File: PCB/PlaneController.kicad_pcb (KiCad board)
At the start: 2 copper layers, 48.3 x 86.4 mm, 12 parts, among them J1 Conn_01x06_Pin, J2 Conn_01x04_Pin, J3 Conn_01x02, M2 Motor_Servo, M3 Motor_Servo, M4 Motor_Servo, M5 Motor_Servo

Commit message: Add 5th servo
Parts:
- added M1: Motor_Servo, Connector_PinHeader_2.54mm:PinHeader_1x03_P2.54mm_Vertical, F.Cu at (96.5, 73.7)
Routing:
- net Net-(A1-D2): track 0.00 -> 12.1 mm
- net Net-(J1-Pin_3): track 166.3 -> 170.7 mm
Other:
- board text added: "D2"

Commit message: Add RX and TX connections to connect to receiver via iBUS
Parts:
- added J4: Conn_01x02, Connector_PinHeader_2.54mm:PinHeader_1x02_P2.54mm_Vertical, F.Cu at (91.4, 99.1)
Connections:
- A1 pad 1: unconnected-(A1-TX1-Pad1) -> Net-(A1-TX1)
- A1 pad 2: unconnected-(A1-RX1-Pad2) -> Net-(A1-RX1)
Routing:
- net Net-(A1-RX1): track 0.00 -> 58.4 mm
- net Net-(A1-TX1): track 0.00 -> 30.9 mm
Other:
- board text added: "RX"
- board text added: "TX"

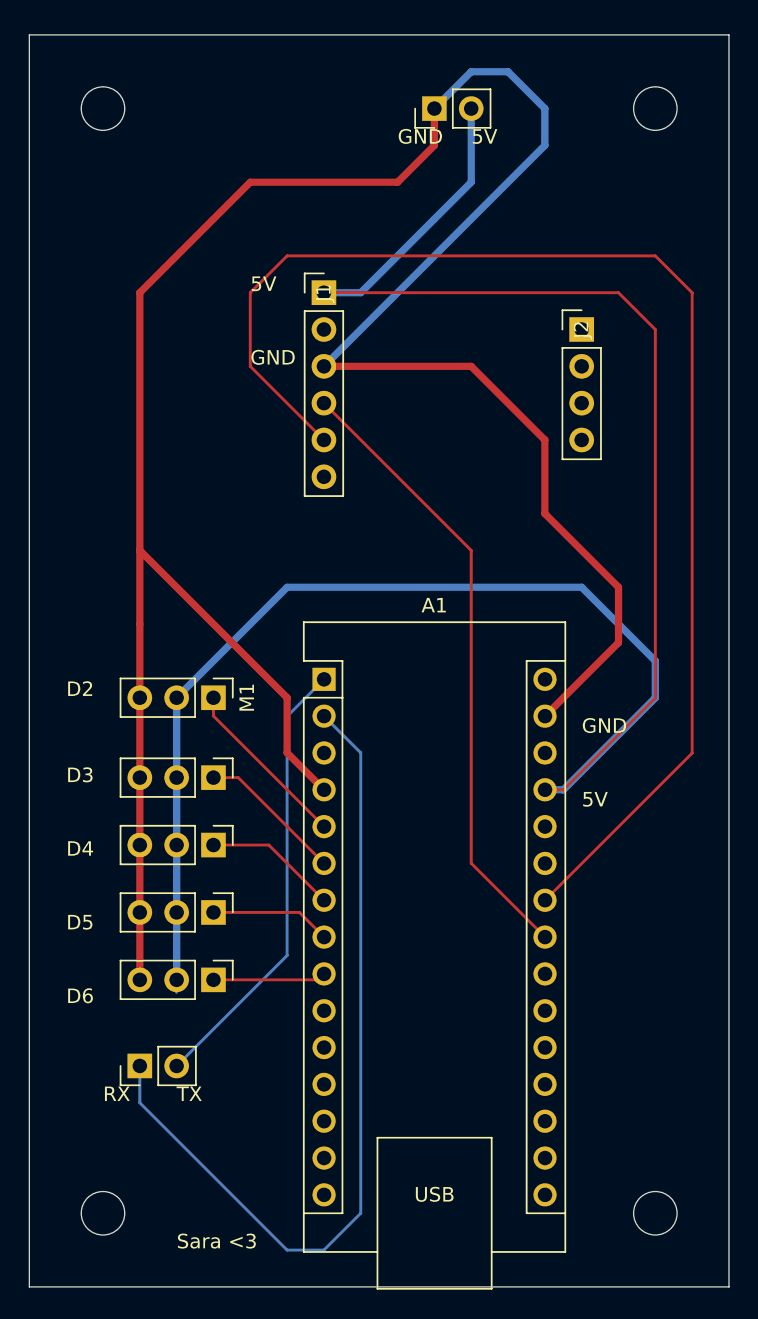
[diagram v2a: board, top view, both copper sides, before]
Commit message: Improve PCB footprint
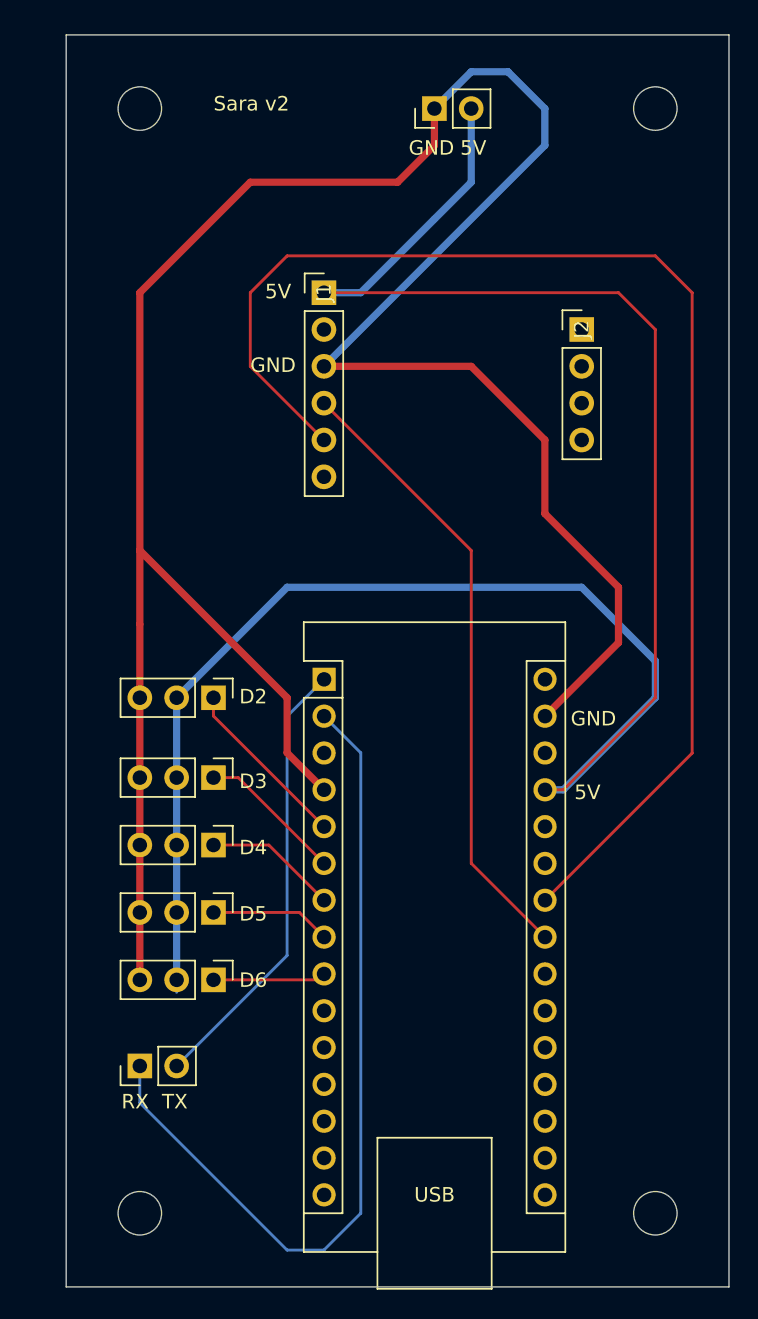
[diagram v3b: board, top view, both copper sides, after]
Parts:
- moved H2 2.54 mm to (91.4, 33.0)
- moved H3 2.54 mm to (91.4, 109.2)
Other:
- board size 48.3 x 86.4 mm -> 45.7 x 86.4 mm
- board text added: "Sara v2"
- board text removed: "Sara <3"
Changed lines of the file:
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@@
 			(at 7.62 -5.08 0)
 			(layer "F.SilkS")
+			(hide yes)
 			(effects
 				(font
@@
 	(footprint "MountingHole:MountingHole_3mm"
 		(layer "F.Cu")
-		(at 88.9 33.02)
+		(at 91.44 33.02)
 		(descr "Mounting Hole 3mm, no annular")
 		(tags "mounting hole 3mm no annular")
@@
 	(footprint "MountingHole:MountingHole_3mm"
 		(layer "F.Cu")
-		(at 88.9 109.22)
+		(at 91.44 109.22)
 		(descr "Mounting Hole 3mm, no annular")
 		(tags "mounting hole 3mm no annular")
@@
 			(at 0 -2.33 90)
 			(layer "F.SilkS")
+			(hide yes)
 			(effects
 				(font
@@
 		)
 		(fp_text user "${REFERENCE}"
-			(at 0 1.27 360)
+			(at 0 1.27 0)
 			(layer "F.Fab")
 			(effects
@@
 			(at 0 4 0)
 			(layer "F.Fab")
+			(hide yes)
 			(effects
 				(font
@@
 	)
 	(gr_rect
-		(start 83.82 27.94)
+		(start 86.36 27.94)
 		(end 132.08 114.3)
 		(stroke
@@
 	)
 	(gr_text "5V"
-		(at 121.92 81.28 0)
+		(at 121.412 80.772 0)
 		(layer "F.SilkS")
 		(effects
@@
 	)
 	(gr_text "D3\n"
-		(at 86.36 79.6 0)
+		(at 98.298 80.01 0)
 		(layer "F.SilkS")
 		(effects
@@
 		)
 	)
-	(gr_text "Sara <3"
-		(at 93.98 111.76 0)
+	(gr_text "Sara v2"
+		(at 96.52 33.274 0)
 		(layer "F.SilkS")
 		(effects
@@
 	)
 	(gr_text "GND"
-		(at 121.92 76.2 0)
+		(at 121.158 75.692 0)
 		(layer "F.SilkS")
 		(effects
@@
 	)
 	(gr_text "RX"
-		(at 88.9 101.6 0)
+		(at 90.17 102.108 0)
 		(layer "F.SilkS")
 		(effects
@@
 	)
 	(gr_text "D6"
-		(at 86.36 94.84 0)
+		(at 98.298 93.726 0)
 		(layer "F.SilkS")
 		(effects
@@
 	)
 	(gr_text "D2\n"
-		(at 86.36 73.66 0)
+		(at 98.298 74.168 0)
 		(layer "F.SilkS")
 		(effects
@@
 	)
 	(gr_text "GND"
-		(at 109.22 35.56 0)
+		(at 109.982 36.322 0)
 		(layer "F.SilkS")
 		(effects
@@
 	)
 	(gr_text "D4"
-		(at 86.36 84.68 0)
+		(at 98.298 84.582 0)
 		(layer "F.SilkS")
 		(effects
@@
 	)
 	(gr_text "TX\n"
-		(at 93.98 101.6 0)
+		(at 92.964 102.108 0)
 		(layer "F.SilkS")
 		(effects
@@
 	)
 	(gr_text "GND"
-		(at 99.06 50.8 0)
+		(at 99.06 51.308 0)
 		(layer "F.SilkS")
 		(effects
@@
 	)
 	(gr_text "5V"
-		(at 99.06 45.72 0)
+		(at 100.076 46.228 0)
 		(layer "F.SilkS")
 		(effects
@@
 	)
 	(gr_text "5V"
-		(at 114.3 35.56 0)
+		(at 113.538 36.322 0)
 		(layer "F.SilkS")
 		(effects
@@
 	)
 	(gr_text "D5\n"
-		(at 86.36 89.76 0)
+		(at 98.298 89.154 0)
 		(layer "F.SilkS")
 		(effects
@@
 		(layer "F.SilkS")
 		(pts
-			(xy 88.9 33.02) (xy 127 33.02)
+			(xy 91.44 33.02) (xy 127 33.02)
 		)
 		(height -12.7)
-		(gr_text "38,1000 mm"
-			(at 107.95 19.22 0)
+		(gr_text "35.5600 mm"
+			(at 109.22 19.22 0)
 			(layer "F.SilkS")
 			(effects
@@
 		(layer "F.SilkS")
 		(pts
-			(xy 86.36 114.3) (xy 86.36 27.94)
+			(xy 86.868 114.3) (xy 86.868 27.94)
 		)
 		(height -12.7)
-		(gr_text "86,3600 mm"
-			(at 72.56 71.12 90)
+		(gr_text "86.3600 mm"
+			(at 73.068 71.12 90)
 			(layer "F.SilkS")
 			(effects
@@
 		(layer "F.SilkS")
 		(pts
-			(xy 132.08 27.94) (xy 83.82 27.94)
+			(xy 132.08 27.94) (xy 86.36 27.94)
 		)
 		(height 12.7)
-		(gr_text "48,2600 mm"
-			(at 107.95 14.14 0)
+		(gr_text "45.7200 mm"
+			(at 109.22 14.14 0)
 			(layer "F.SilkS")
 			(effects
@@
 		)
 		(height -10.16)
-		(gr_text "76,2000 mm"
+		(gr_text "76.2000 mm"
 			(at 136.06 71.12 90)
 			(layer "F.SilkS")

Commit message: Add connection to receiver using 3x1 pin for iBUS, Vcc and GND
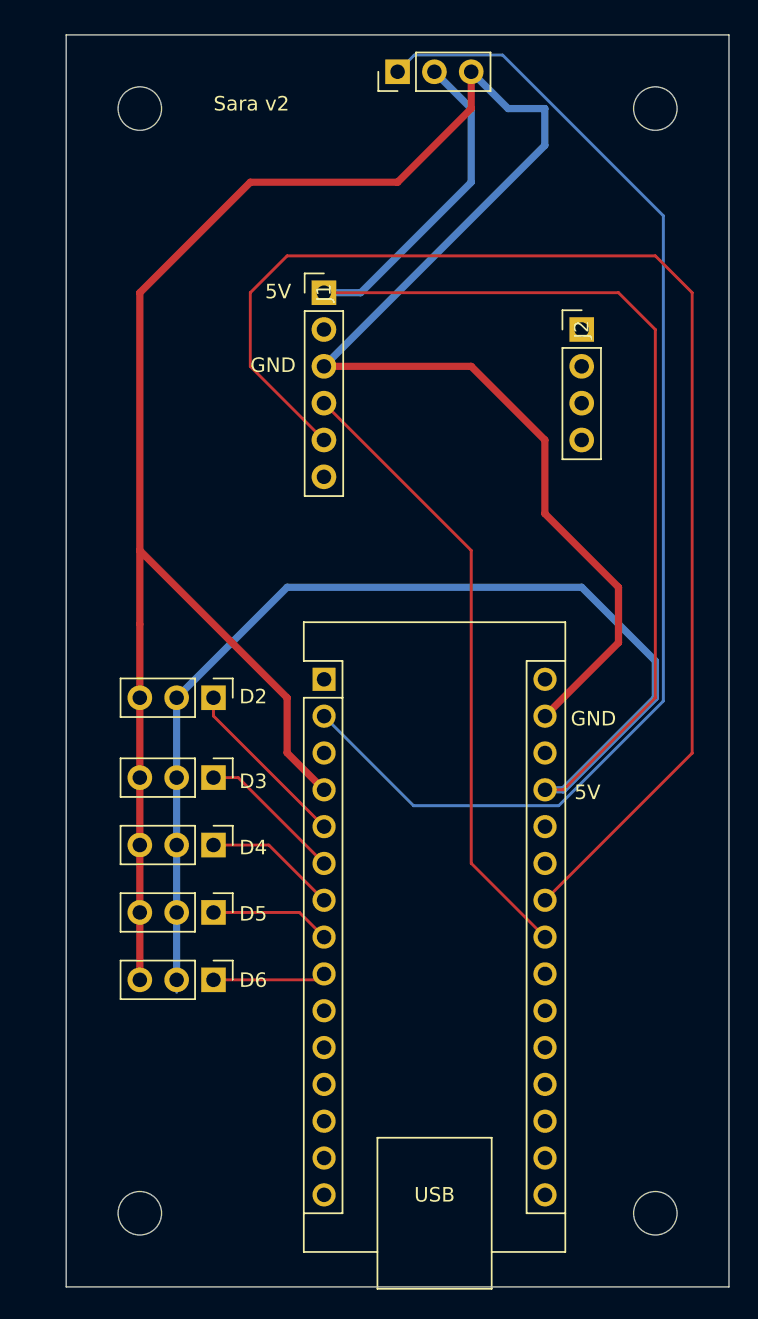
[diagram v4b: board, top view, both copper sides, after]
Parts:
- removed J4: Conn_01x02, Connector_PinHeader_2.54mm:PinHeader_1x02_P2.54mm_Vertical
- J3: value Conn_01x02 -> Conn_01x03; footprint Connector_PinHeader_2.54mm:PinHeader_1x02_P2.54mm_Vertical -> Connector_PinHeader_2.54mm:PinHeader_1x03_P2.54mm_Vertical
- moved J3 3.59 mm to (109.2, 30.5)
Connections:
- A1 pad 1: Net-(A1-TX1) -> unconnected-(A1-TX1-Pad1)
- J3 pad 1: Net-(J1-Pin_3) -> Net-(A1-RX1)
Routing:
- net Net-(A1-TX1): track 30.9 -> 0.00 mm
- net Net-(A1-RX1): track 58.4 -> 85.8 mm
- net Net-(A1-+5V): track 149.3 -> 152.9 mm
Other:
- board text removed: "RX"
- board text removed: "TX"

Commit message: Add PCB traces for CC1101 radio
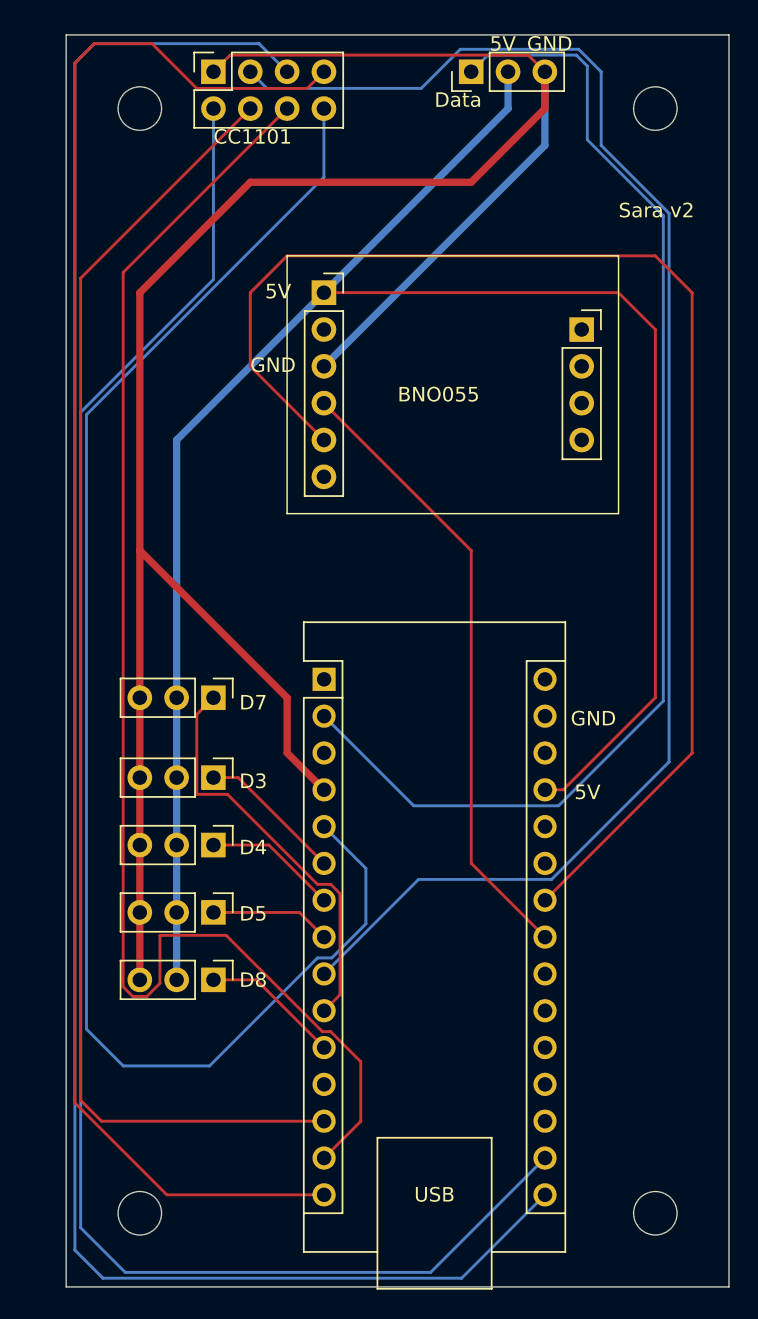
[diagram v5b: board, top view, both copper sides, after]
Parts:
- added J4: Conn_02x04_Odd_Even, Connector_PinSocket_2.54mm:PinSocket_2x04_P2.54mm_Vertical, F.Cu at (96.5, 30.5)
- J1: footprint Connector_PinHeader_2.54mm:PinHeader_1x06_P2.54mm_Vertical -> Connector_PinSocket_2.54mm:PinSocket_1x06_P2.54mm_Vertical
- J2: footprint Connector_PinHeader_2.54mm:PinHeader_1x04_P2.54mm_Vertical -> Connector_PinSocket_2.54mm:PinSocket_1x04_P2.54mm_Vertical
- moved J3 5.08 mm to (114.3, 30.5)
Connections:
- net Net-(J1-Pin_3) renamed /GND
- A1 pad 10: unconnected-(A1-D7-Pad10) -> Net-(A1-D7)
- A1 pad 11: unconnected-(A1-D8-Pad11) -> Net-(A1-D8)
- A1 pad 13: unconnected-(A1-D10-Pad13) -> /CSN
- A1 pad 14: unconnected-(A1-MOSI-Pad14) -> /MOSI
- A1 pad 15: unconnected-(A1-MISO-Pad15) -> /MISO
- A1 pad 16: unconnected-(A1-SCK-Pad16) -> /SCK
- A1 pad 17: unconnected-(A1-3V3-Pad17) -> /3.3V
- A1 pad 5: Net-(A1-D2) -> /GDO2
- A1 pad 9: Net-(A1-D6) -> /GDO1
- M1 pad 1: Net-(A1-D2) -> Net-(A1-D7)
- M5 pad 1: Net-(A1-D6) -> Net-(A1-D8)
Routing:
- net /SCK: track 0.00 -> 133.5 mm
- net /3.3V: track 0.00 -> 117.6 mm
- net /MISO: track 0.00 -> 111.0 mm
- net /GDO1: track 0.00 -> 105.8 mm
- net /GDO2: track 0.00 -> 102.6 mm
- net /MOSI: track 0.00 -> 96.9 mm
- net /CSN: track 0.00 -> 90.6 mm
- net Net-(A1-D7): track 0.00 -> 28.4 mm
- net Net-(A1-+5V): track 152.9 -> 131.7 mm
- net /GND: track 170.7 -> 155.4 mm
- net Net-(A1-D2): track 12.1 -> 0.00 mm
- net Net-(A1-D8): track 0.00 -> 9.56 mm
- net Net-(A1-D6): track 7.80 -> 0.00 mm
- net Net-(A1-RX1): track 85.8 -> 83.7 mm
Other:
- board text added: "BNO055"
- board text added: "CC1101"
- board text added: "D7"
- board text added: "D8"
- board text added: "Data"
- board text removed: "D2"
- board text removed: "D6"
